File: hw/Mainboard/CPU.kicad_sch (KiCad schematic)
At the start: 10 parts, among them U11 W65C02S, U12 AS6C1008

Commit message: jlcpcb - 1/19
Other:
- note added: "A single SRAM chip is used for system RAM, video RAM, and ROM. The ROM portion is initialized at POR by the MCU."
- note added: "RAM_A[10..11] are used to mirror the screen RAM when the CPU accesses range $8000-8FFF. 40 col PET has 1k of screen RAM, mirrored 4 times. 80 col PET has 2k of screen RAM, mirrored 2 times."
- note added: "To improve routing, A[0..16] and D[0..7] and arbitrarily assigned to the address and data pins of the SRAM."
- note added: "To reduce/simplify level shifting, CPU and RAM operate at +3V3 to interface directly with the FPGA."
- note removed: "To improve routing, A[0..16] and D[0..7] and arbitrarily assigned to the address and data pins of the SRAM. RAM_A[10..11] are used to mirror the screen RAM when the CPU accesses range $8000-8FFF. 40 col PET has 1k of screen RAM, mirrored 4 times. 80 col PET has 2k of screen RAM, mirrored 2 times."
- title: (none) -> CPU & RAM
- moved on the sheet: C10, C11, R38, R39, R40, R59, U11, U12

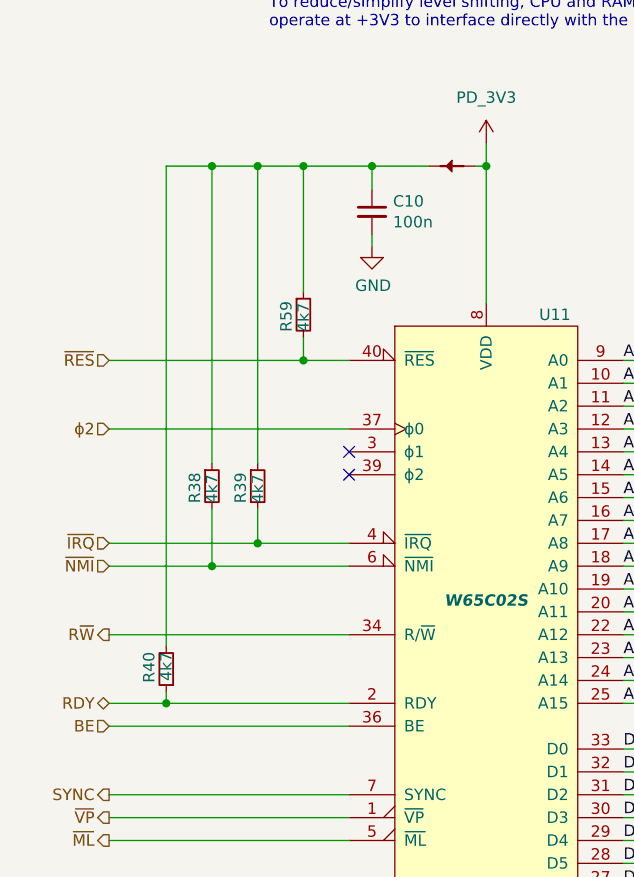
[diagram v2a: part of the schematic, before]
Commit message: hw: RDY should be series resistor instead of pullup
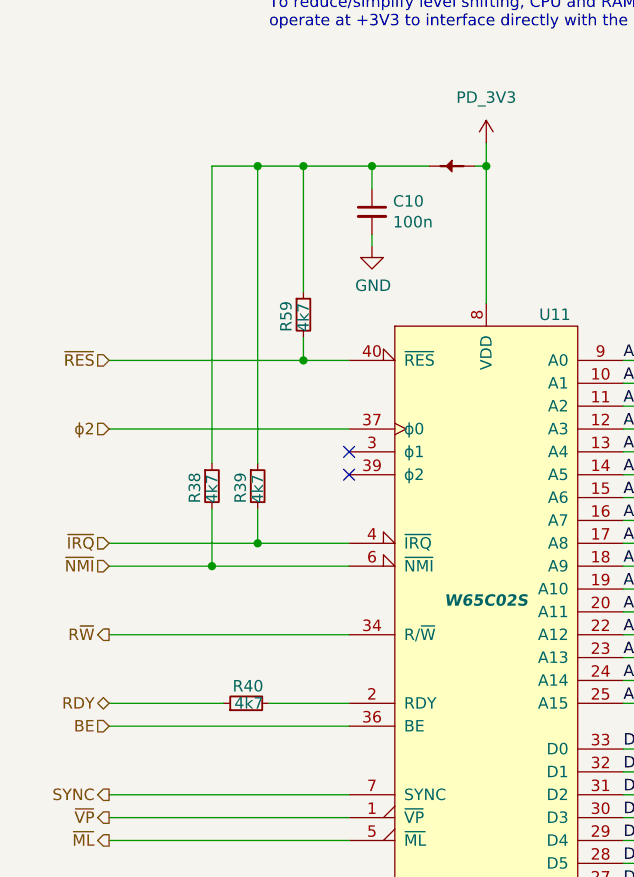
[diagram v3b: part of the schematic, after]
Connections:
- net RDY: no longer U11.2 (RDY)
- net at C10.1, PT1.2, R38.1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: no longer R40.2
- new net: R40.2, U11.2 (RDY)
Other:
- moved on the sheet: R40
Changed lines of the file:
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@@
   (junction (at 139.7 125.73) (diameter 0) (color 0 0 0 0)
   )
-  (junction (at 124.46 163.83) (diameter 0) (color 0 0 0 0)
-  )
   (junction (at 139.7 104.14) (diameter 0) (color 0 0 0 0)
-  )
-  (junction (at 129.54 104.14) (diameter 0) (color 0 0 0 0)
   )
   (junction (at 160.02 104.14) (diameter 0) (color 0 0 0 0)
@@
     (stroke (width 0) (type default) (color 0 0 0 0))
   )
-  (wire (pts (xy 124.46 104.14) (xy 124.46 157.48))
-    (stroke (width 0) (type default) (color 0 0 0 0))
-  )
   (wire (pts (xy 144.78 166.37) (xy 118.11 166.37))
     (stroke (width 0) (type default) (color 0 0 0 0))
@@
     (stroke (width 0) (type default) (color 0 0 0 0))
   )
+  (wire (pts (xy 135.89 163.83) (xy 144.78 163.83))
+    (stroke (width 0) (type default) (color 0 0 0 0))
+  )
   (bus (pts (xy 203.2 133.35) (xy 203.2 135.89))
     (stroke (width 0) (type default) (color 0 0 0 0))
@@
     (stroke (width 0) (type default) (color 0 0 0 0))
   )
-  (wire (pts (xy 124.46 163.83) (xy 118.11 163.83))
+  (wire (pts (xy 118.11 163.83) (xy 130.81 163.83))
     (stroke (width 0) (type default) (color 0 0 0 0))
   )
@@
     (stroke (width 0) (type default) (color 0 0 0 0))
   )
-  (wire (pts (xy 129.54 104.14) (xy 124.46 104.14))
-    (stroke (width 0) (type default) (color 0 0 0 0))
-  )
   (bus (pts (xy 181.61 148.59) (xy 181.61 151.13))
     (stroke (width 0) (type default) (color 0 0 0 0))
@@
     (stroke (width 0) (type default) (color 0 0 0 0))
   )
-  (wire (pts (xy 124.46 163.83) (xy 144.78 163.83))
-    (stroke (width 0) (type default) (color 0 0 0 0))
-  )
   (wire (pts (xy 205.74 146.05) (xy 242.57 146.05))
     (stroke (width 0) (type default) (color 0 0 0 0))
@@
   )
   (wire (pts (xy 118.11 146.05) (xy 134.62 146.05))
-    (stroke (width 0) (type default) (color 0 0 0 0))
-  )
-  (wire (pts (xy 124.46 162.56) (xy 124.46 163.83))
     (stroke (width 0) (type default) (color 0 0 0 0))
   )
@@
     (pin "2")
   )
-  (symbol (lib_id "Device:R_Small") (at 124.46 160.02 180) (unit 1)
+  (symbol (lib_id "Device:R_Small") (at 133.35 163.83 90) (unit 1)
     (in_bom yes) (on_board yes)
-    (property "Reference" "R40" (id 0) (at 122.555 158.115 90)
+    (property "Reference" "R40" (id 0) (at 135.255 161.925 90)
       (effects (font (size 1.27 1.27)) (justify left))
     )
-    (property "Value" "4k7" (id 1) (at 124.46 158.115 90)
+    (property "Value" "4k7" (id 1) (at 135.255 163.83 90)
       (effects (font (size 1.27 1.27)) (justify left))
     )
-    (property "Footprint" "Resistor_SMD:R_0402_1005Metric" (id 2) (at 124.46 160.02 0)
-      (effects (font (size 1.27 1.27)) hide)
-    )
-    (property "Datasheet" "https://datasheet.lcsc.com/lcsc/2206010045_UNI-ROYAL-Uniroyal-Elec-0402WGF4701TCE_C25900.pdf" (id 3) (at 124.46 160.02 0)
-      (effects (font (size 1.27 1.27)) hide)
-    )
-    (property "LCSC" "C25900" (id 4) (at 124.46 160.02 0)
-      (effects (font (size 1.27 1.27)) hide)
-    )
+    (property "Footprint" "Resistor_SMD:R_0402_1005Metric" (id 2) (at 133.35 163.83 0)
+      (effects (font (size 1.27 1.27)) hide)
+    )
+    (property "Datasheet" "https://datasheet.lcsc.com/lcsc/2206010045_UNI-ROYAL-Uniroyal-Elec-0402WGF4701TCE_C25900.pdf" (id 3) (at 133.35 163.83 0)
+      (effects (font (size 1.27 1.27)) hide)
+    )
+    (property "LCSC" "C25900" (id 4) (at 133.35 163.83 0)
+      (effects (font (size 1.27 1.27)) hide)
+    )

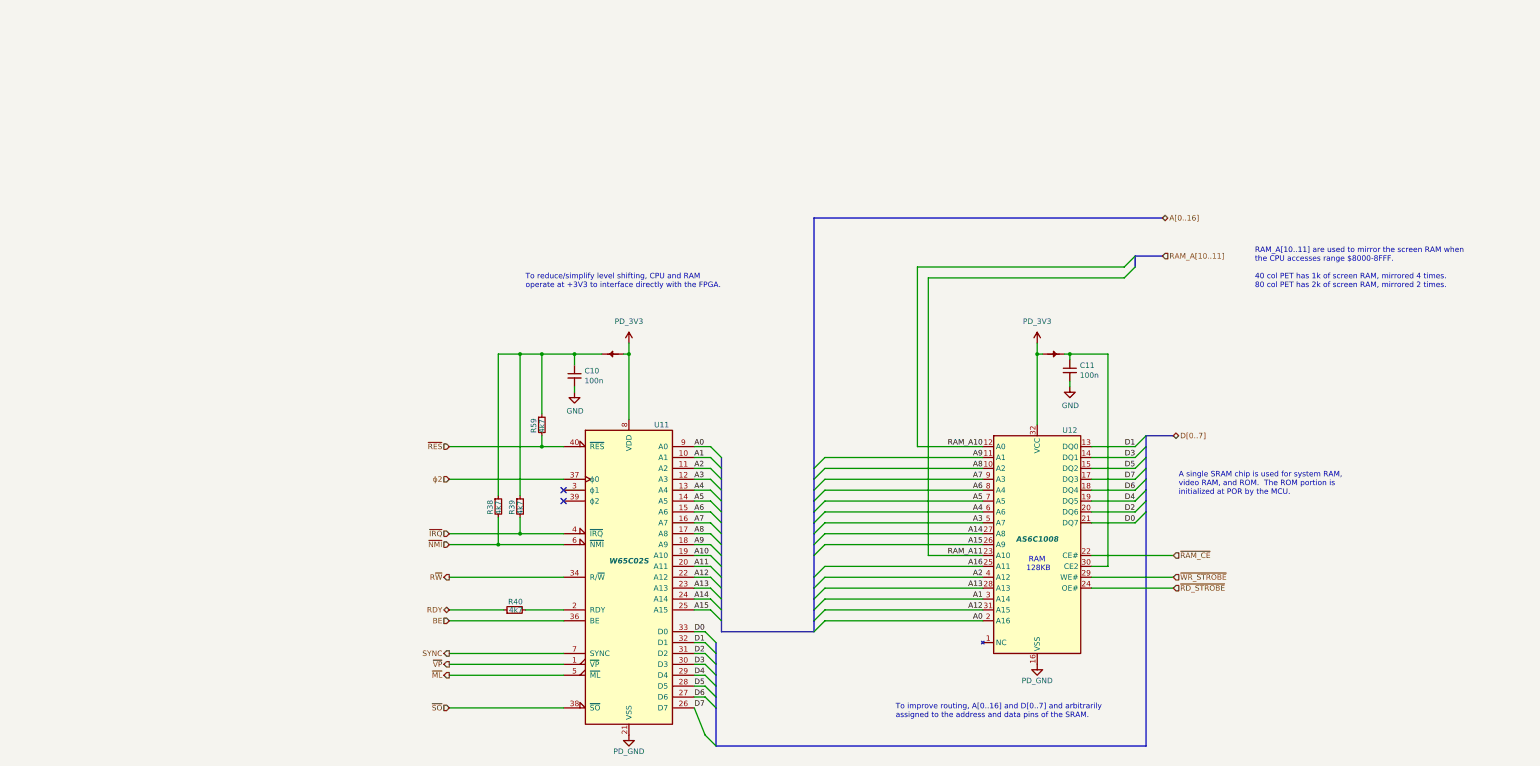
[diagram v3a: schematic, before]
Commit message: hw: tidy power and resize pages
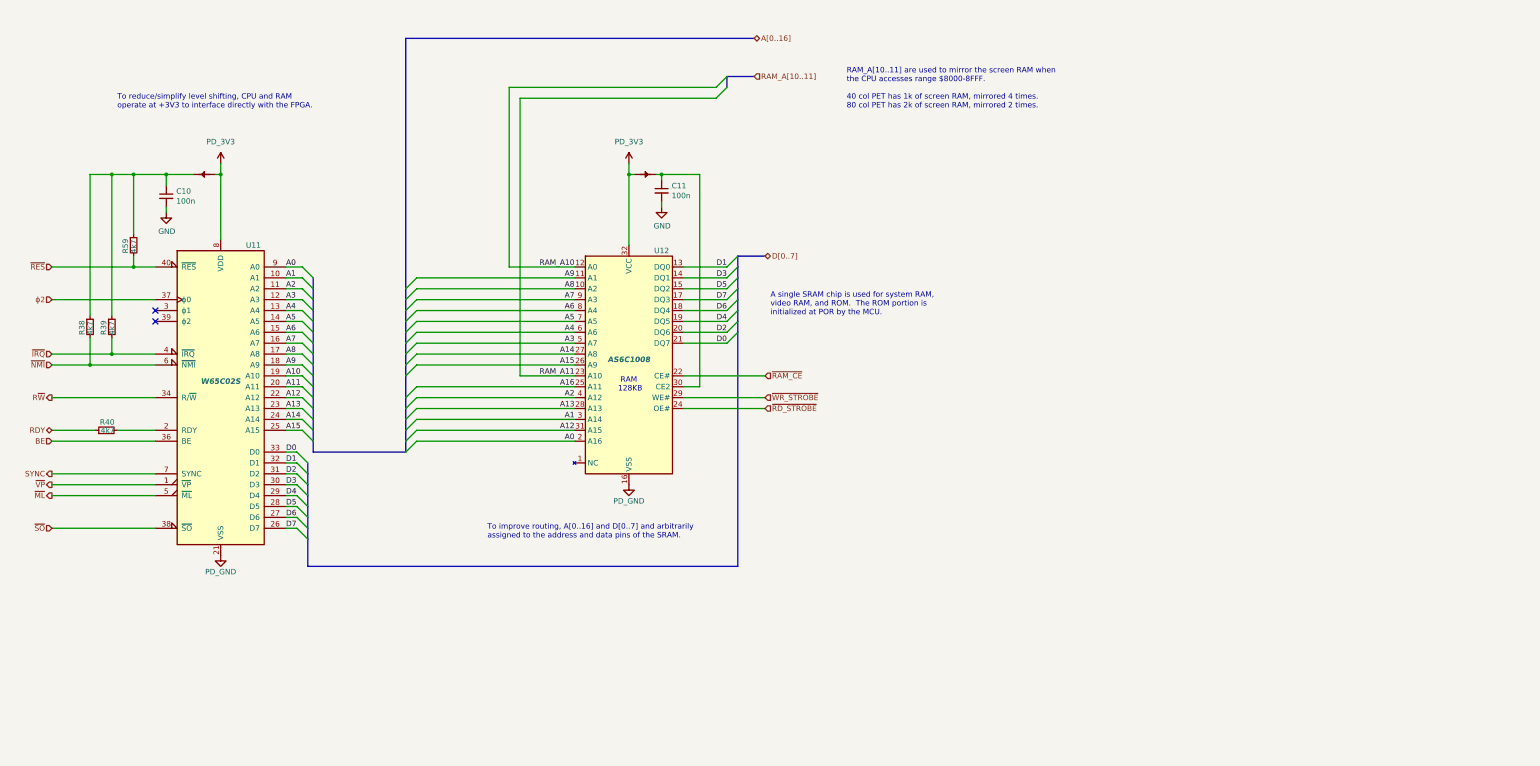
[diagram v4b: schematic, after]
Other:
- title: CPU & RAM -> CBM PET Mainboard Replacement
- moved on the sheet: C10, C11, R38, R39, R40, R59, U11, U12

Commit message: hw: tidy CPU, rename RD/WR strobe to RAM_OE/_WE, debounce switches
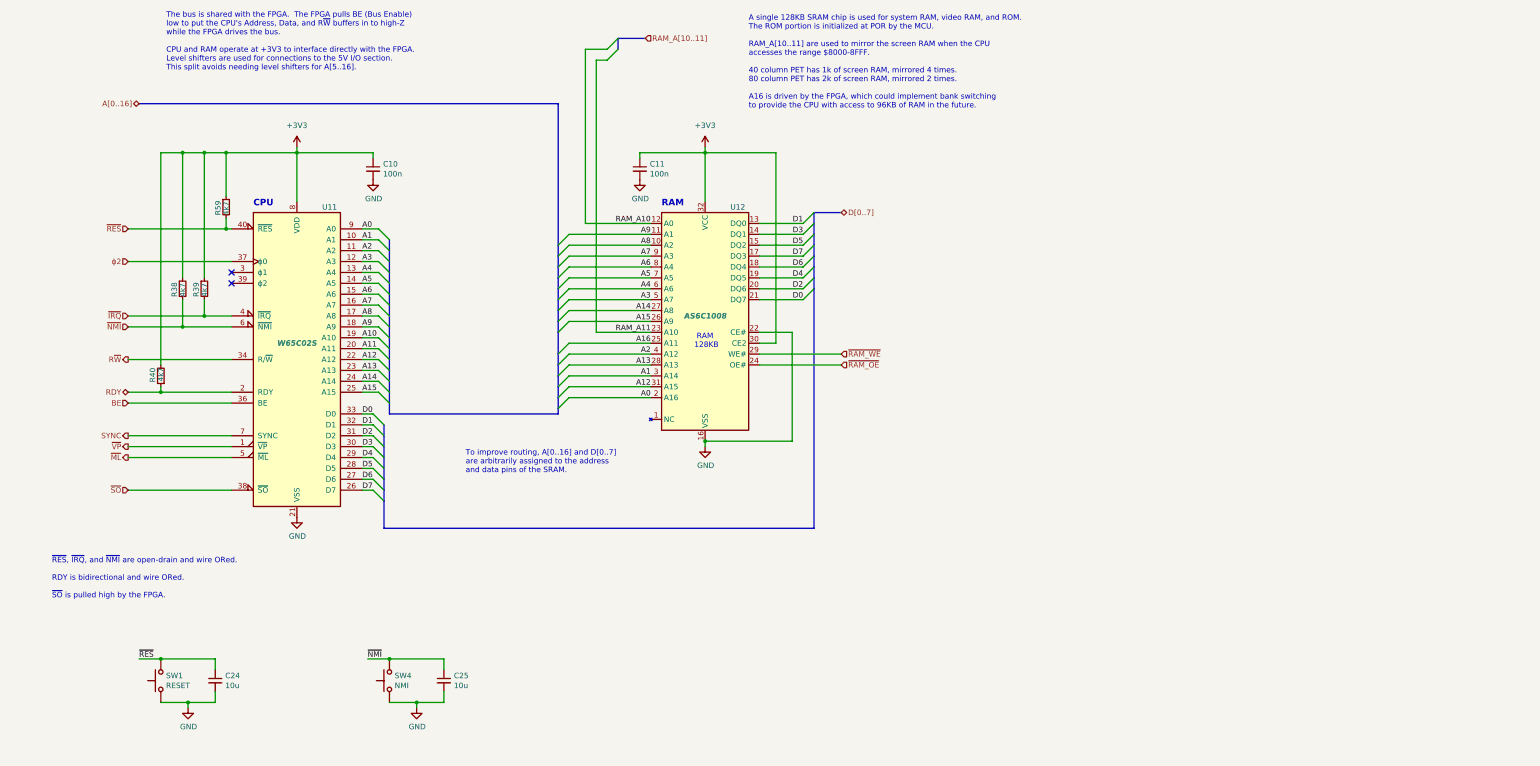
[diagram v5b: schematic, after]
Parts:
- removed PT1, PT2: PowerTie_2, PET:NetTie-2_SMD_Pad_1.6_to_0.4mm, symbol PET:PowerTie_2
- added C24, C25: 10u, Capacitor_SMD:C_0603_1608Metric, symbol Device:C_Small
- added SW1: RESET, JLCPCB:SW-TH_L6.0-W3.5-P6.50, symbol Switch:SW_Push
- added SW4: NMI, JLCPCB:SW-TH_L6.0-W3.5-P6.50, symbol Switch:SW_Push
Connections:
- net PD_3V3 is gone; now on net +3V3: U11.8 (VDD), U12.32 (VCC)
- net PD_GND is gone; now on net GND: U11.21 (VSS), U12.16 (VSS)
- net ~{RAM_CE} is gone; now on net GND: U12.22 (CE#)
- net GND: now also C24.2, C25.2, SW1.1, SW4.1
- net RDY: now also U11.2 (RDY)
- net ~{NMI}: now also C25.1, SW4.2
- net ~{RES}: now also C24.1, SW1.2
- net +3V3: now reaches R40.2
- net +3V3: now also C10.1, C11.1, R38.1, R39.1, R59.1, U12.30 (CE2); no longer U11.2 (RDY)
- net ~{RD_STROBE} renamed ~{RAM_OE}
- net ~{WR_STROBE} renamed ~{RAM_WE}
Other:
- note added: "A single 128KB SRAM chip is used for system RAM, video RAM, and ROM. The ROM portion is initialized at POR by the MCU. RAM_A[10..11] are used to mirror the screen RAM when the CPU accesses the range $8000-8FFF. 40 column PET has 1k of screen RAM, mirrored 4 times. 80 column PET has 2k of screen RAM, mirrored 2 times. A16 is driven by the FPGA, which could implement bank switching to provide the C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"
- note added: "CPU"
- note added: "RAM"
- note added: "The bus is shared with the FPGA. The FPGA pulls BE (Bus Enable) low to put the CPU's Address, Data, and R~{W} buffers in to high-Z while the FPGA drives the bus. CPU and RAM operate at +3V3 to interface directly with the FPGA. Level shifters are used for connections to the 5V I/O section. This split avoids needing level shifters for A[5..16]."
- note added: "To improve routing, A[0..16] and D[0..7] are arbitrarily assigned to the address and data pins of the SRAM."
- note added: "~{RES}, ~{IRQ}, and ~{NMI} are open-drain and wire ORed. RDY is bidirectional and wire ORed. ~{SO} is pulled high by the FPGA."
- note removed: "A single SRAM chip is used for system RAM, video RAM, and ROM. The ROM portion is initialized at POR by the MCU."
- note removed: "RAM_A[10..11] are used to mirror the screen RAM when the CPU accesses range $8000-8FFF. 40 col PET has 1k of screen RAM, mirrored 4 times. 80 col PET has 2k of screen RAM, mirrored 2 times."
- note removed: "To improve routing, A[0..16] and D[0..7] and arbitrarily assigned to the address and data pins of the SRAM."
- note removed: "To reduce/simplify level shifting, CPU and RAM operate at +3V3 to interface directly with the FPGA."
- moved on the sheet: C10, C11, R38, R39, R40, R59, U11, U12

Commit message: hw: tidy IO, move CPU decoupling caps
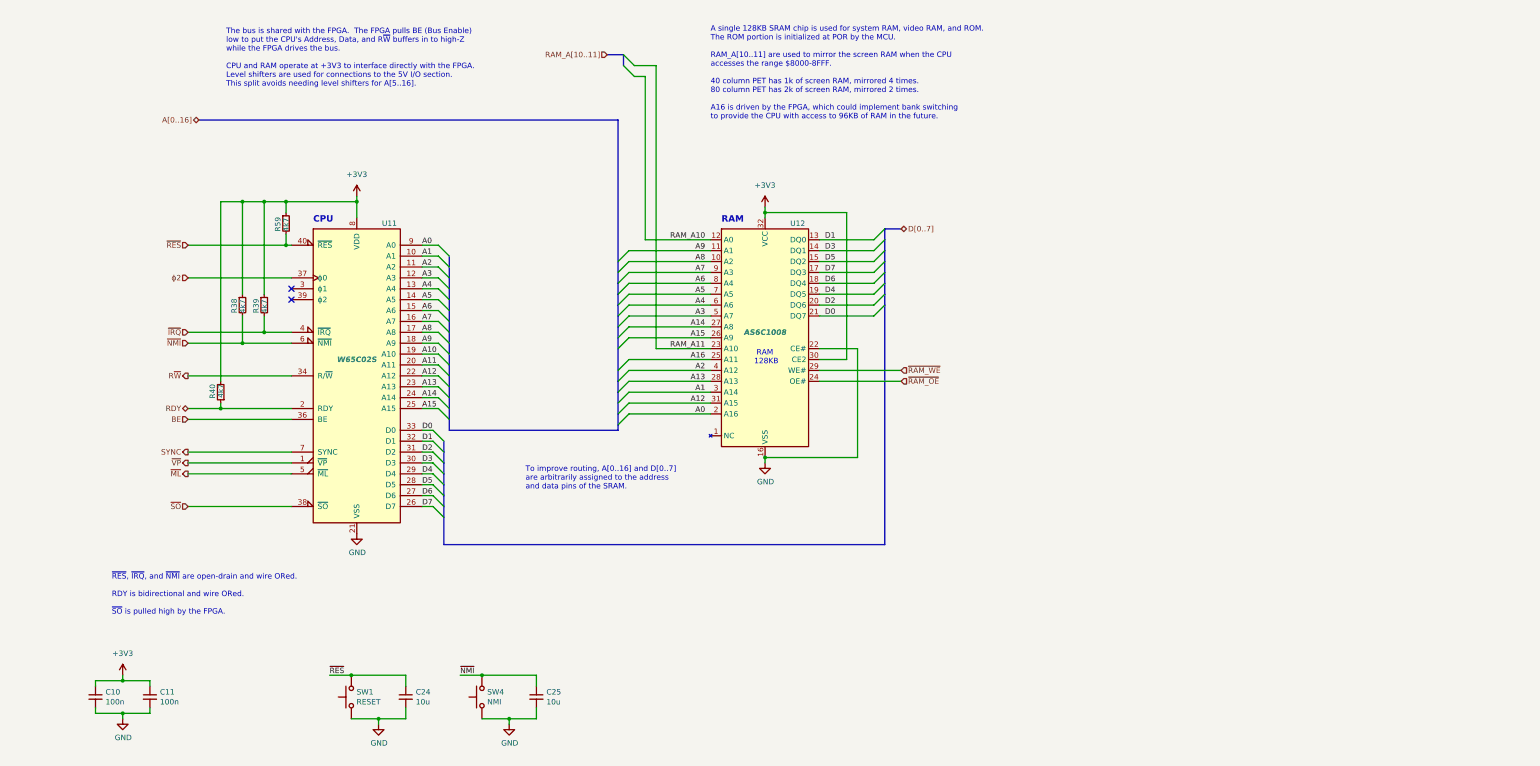
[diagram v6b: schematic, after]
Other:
- moved on the sheet: C10, C11, C24, C25, R38, R39, R40, R59, SW1, SW4, U11, U12
